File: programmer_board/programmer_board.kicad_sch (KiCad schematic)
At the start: 18 parts, among them J1 8bit_thing_bus_connector, J2 greenpak_i2c, U1 Pico, U2 74AHCT573, U3 74AHCT573, U4 74AHCT573, U5 74LVC245, U6 SLG46826G

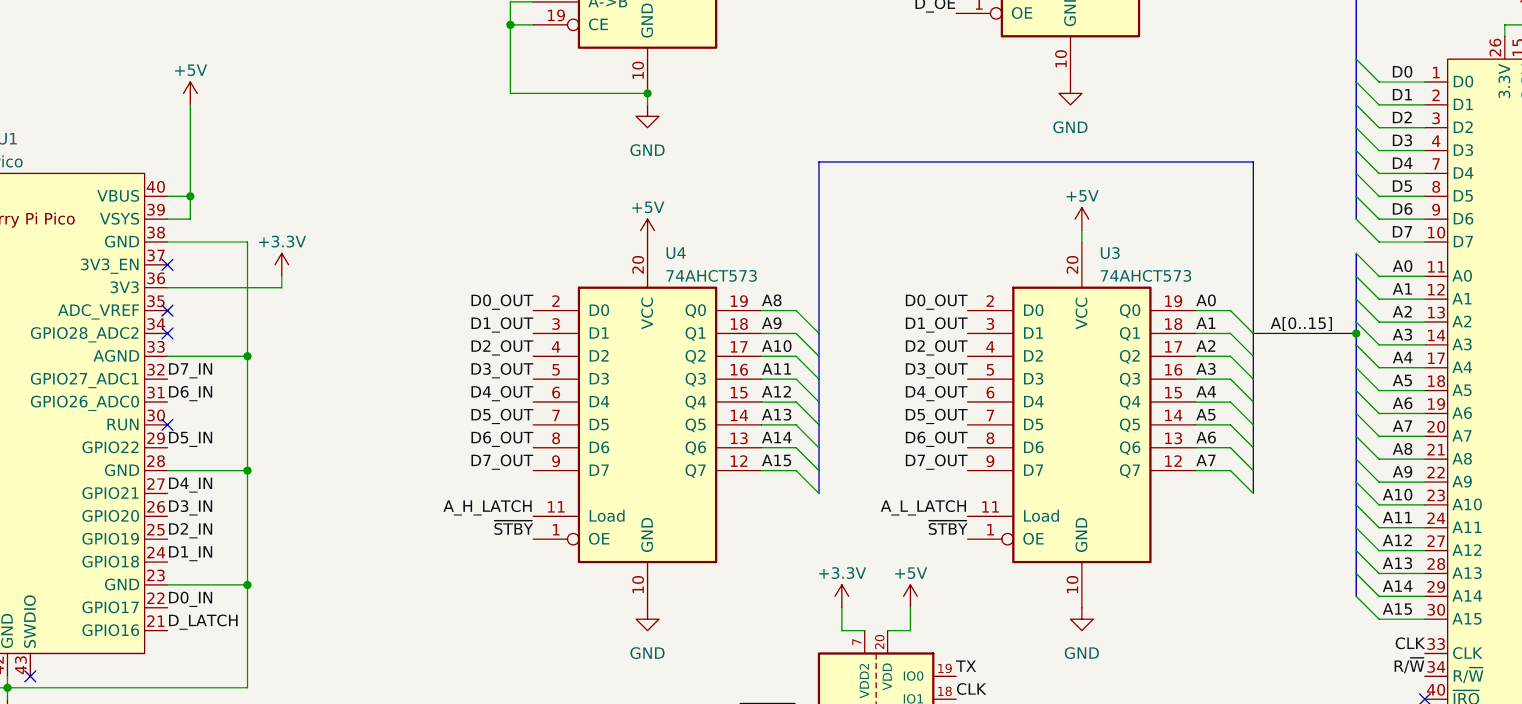
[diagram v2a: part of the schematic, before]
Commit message: pico board: low address latch needs independent OE to not conflict with latch on HD6301 board
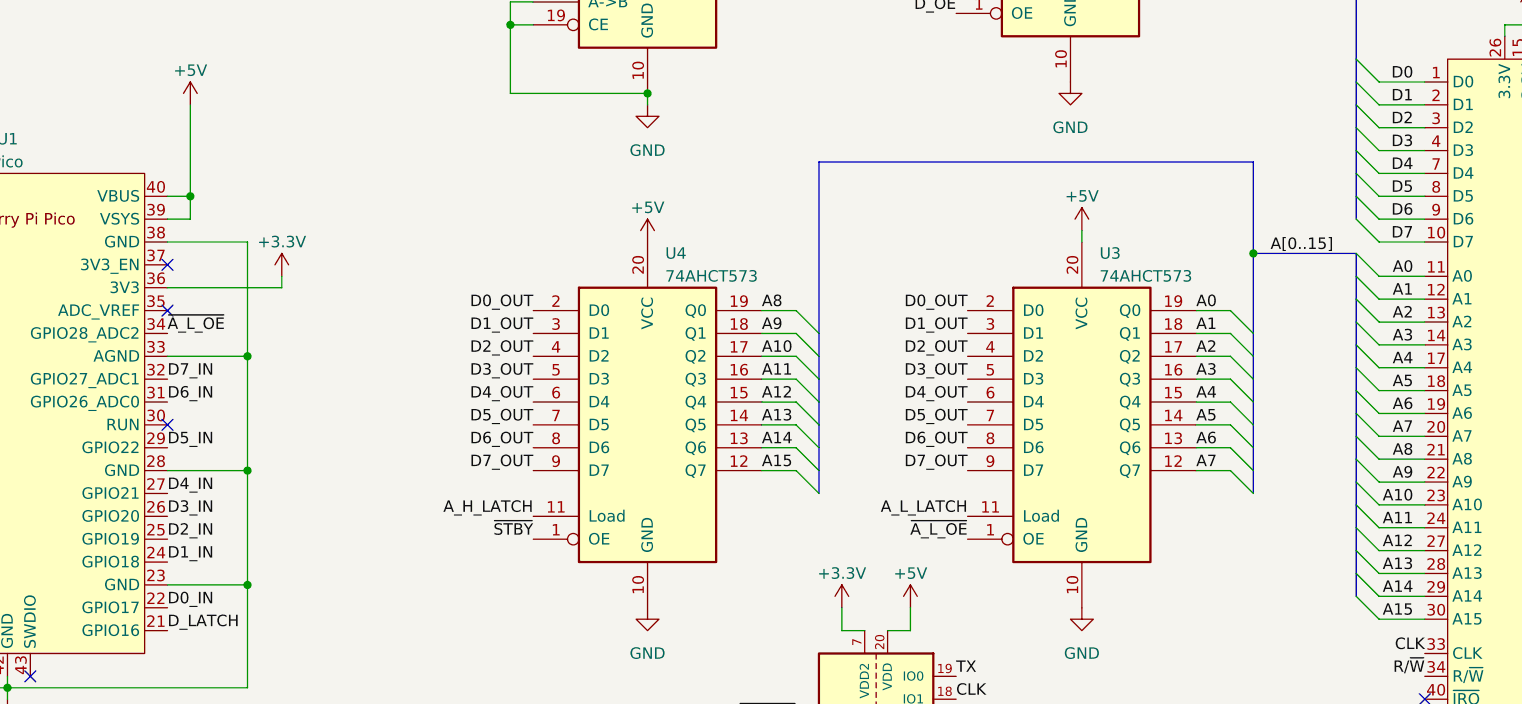
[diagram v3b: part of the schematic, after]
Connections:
- net ~{STBY}: no longer U3.1 (OE)
- net ~{A_L_OE}: now reaches U1.34 (GPIO28_ADC2)
- net ~{A_L_OE}: now also U3.1 (OE)
- no-connect marks 10 -> 9
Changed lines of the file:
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@@
   (junction (at 139.7 57.15) (diameter 0) (color 0 0 0 0)
   )
-  (junction (at 233.68 91.44) (diameter 0) (color 0 0 0 0)
-  )
   (junction (at 252.73 57.15) (diameter 0) (color 0 0 0 0)
   )
@@
   )
   (junction (at 72.39 26.67) (diameter 0) (color 0 0 0 0)
+  )
+  (junction (at 222.25 82.55) (diameter 0) (color 0 0 0 0)
   )
   (junction (at 257.81 57.15) (diameter 0) (color 0 0 0 0)
@@
   (no_connect (at 241.3 134.62))
   (no_connect (at 81.28 129.54))
-  (no_connect (at 101.6 91.44))
   (bus_entry (at 233.68 78.74) (size 2.54 2.54)
     (stroke (width 0) (type default))
@@
     (stroke (width 0) (type default))
   )
-  (bus (pts (xy 222.25 91.44) (xy 233.68 91.44))
+  (bus (pts (xy 222.25 82.55) (xy 233.68 82.55))
     (stroke (width 0) (type default))
   )
@@
     (stroke (width 0) (type default))
   )
-  (bus (pts (xy 233.68 90.17) (xy 233.68 91.44))
-    (stroke (width 0) (type default))
-  )
   (bus (pts (xy 233.68 92.71) (xy 233.68 95.25))
     (stroke (width 0) (type default))
@@
     (stroke (width 0) (type default))
   )
-  (bus (pts (xy 233.68 91.44) (xy 233.68 92.71))
+  (bus (pts (xy 233.68 90.17) (xy 233.68 92.71))
     (stroke (width 0) (type default))
   )
@@
     (stroke (width 0) (type default))
   )
+  (bus (pts (xy 222.25 82.55) (xy 222.25 72.39))
+    (stroke (width 0) (type default))
+  )
   (wire (pts (xy 236.22 87.63) (xy 241.3 87.63))
     (stroke (width 0) (type default))
@@
     (stroke (width 0) (type default))
   )
-  (bus (pts (xy 222.25 91.44) (xy 222.25 72.39))
+  (bus (pts (xy 222.25 91.44) (xy 222.25 82.55))
     (stroke (width 0) (type default))
   )
@@
     (effects (font (size 1.27 1.27)) (justify right bottom))
   )
-  (label "A[0..15]" (at 231.14 91.44 180) (fields_autoplaced)
+  (label "A[0..15]" (at 231.14 82.55 180) (fields_autoplaced)
     (effects (font (size 1.27 1.27)) (justify right bottom))
   )
@@
     (effects (font (size 1.27 1.27)) (justify left bottom))
   )
+  (label "~{A_L_OE}" (at 101.6 91.44 0) (fields_autoplaced)
+    (effects (font (size 1.27 1.27)) (justify left bottom))
+  )
   (label "P_CLK" (at 171.45 137.16 180) (fields_autoplaced)
     (effects (font (size 1.27 1.27)) (justify right bottom))
@@
     (effects (font (size 1.27 1.27)) (justify right bottom))
   )
-  (label "~{STBY}" (at 190.5 114.3 180) (fields_autoplaced)
-    (effects (font (size 1.27 1.27)) (justify right bottom))
-  )
   (label "P_TX" (at 66.04 76.2 180) (fields_autoplaced)
     (effects (font (size 1.27 1.27)) (justify right bottom))
@@
     (effects (font (size 1.27 1.27)) (justify right bottom))
   )
+  (label "~{A_L_OE}" (at 190.5 114.3 180) (fields_autoplaced)
+    (effects (font (size 1.27 1.27)) (justify right bottom))
+  )

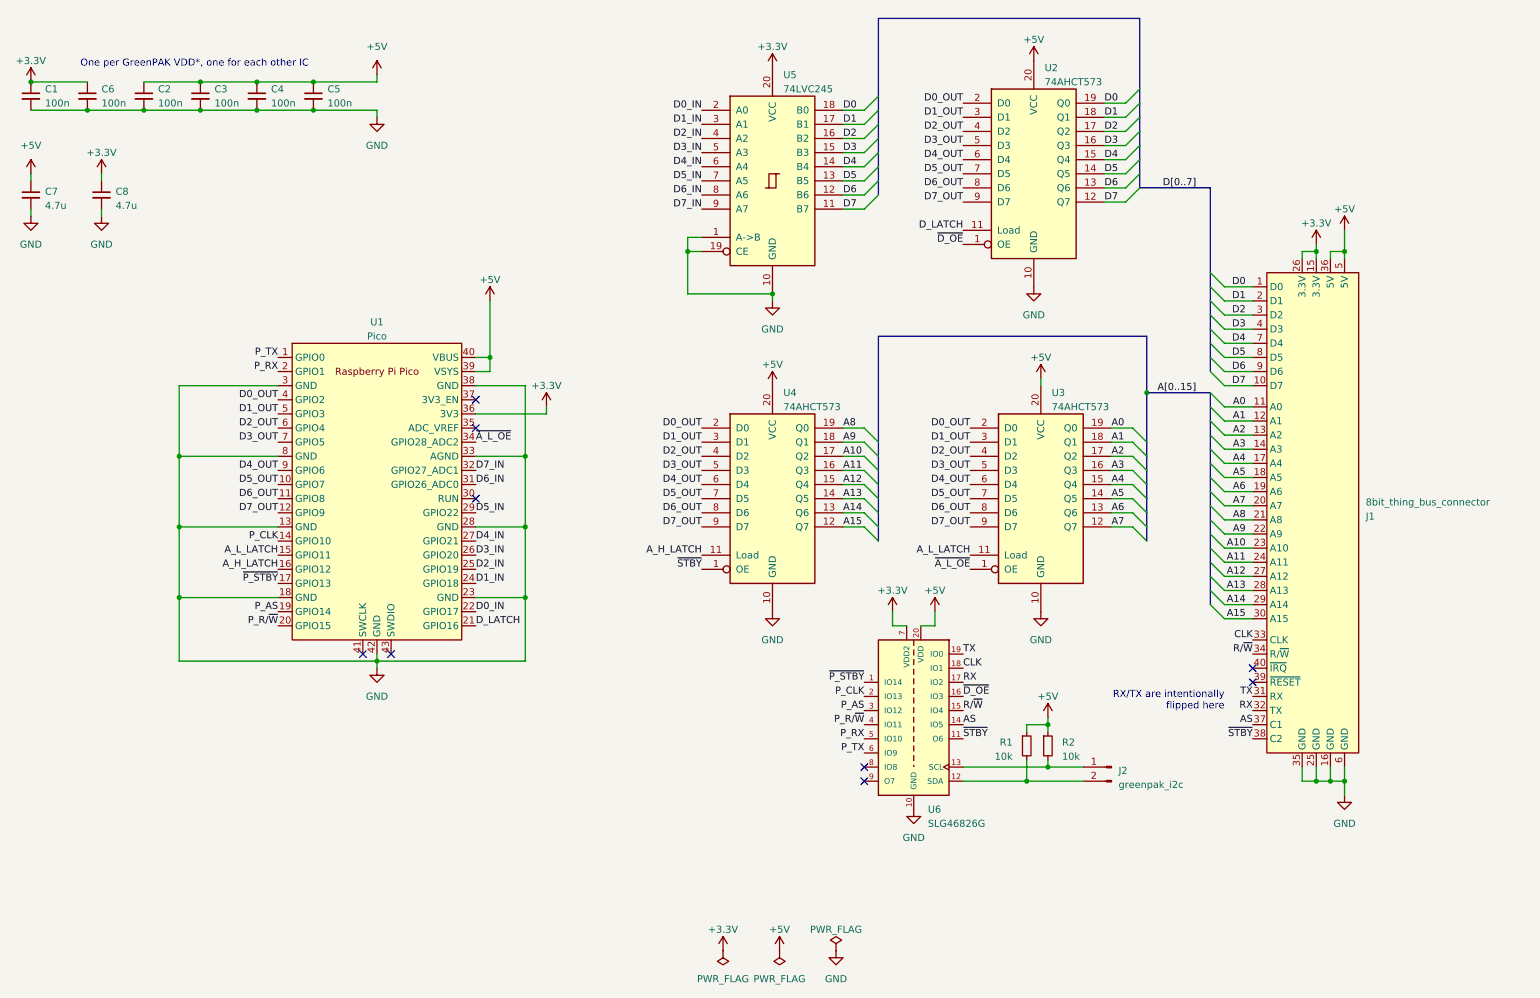
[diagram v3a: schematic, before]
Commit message: Completely reworked Pico programmer v1 board - final version
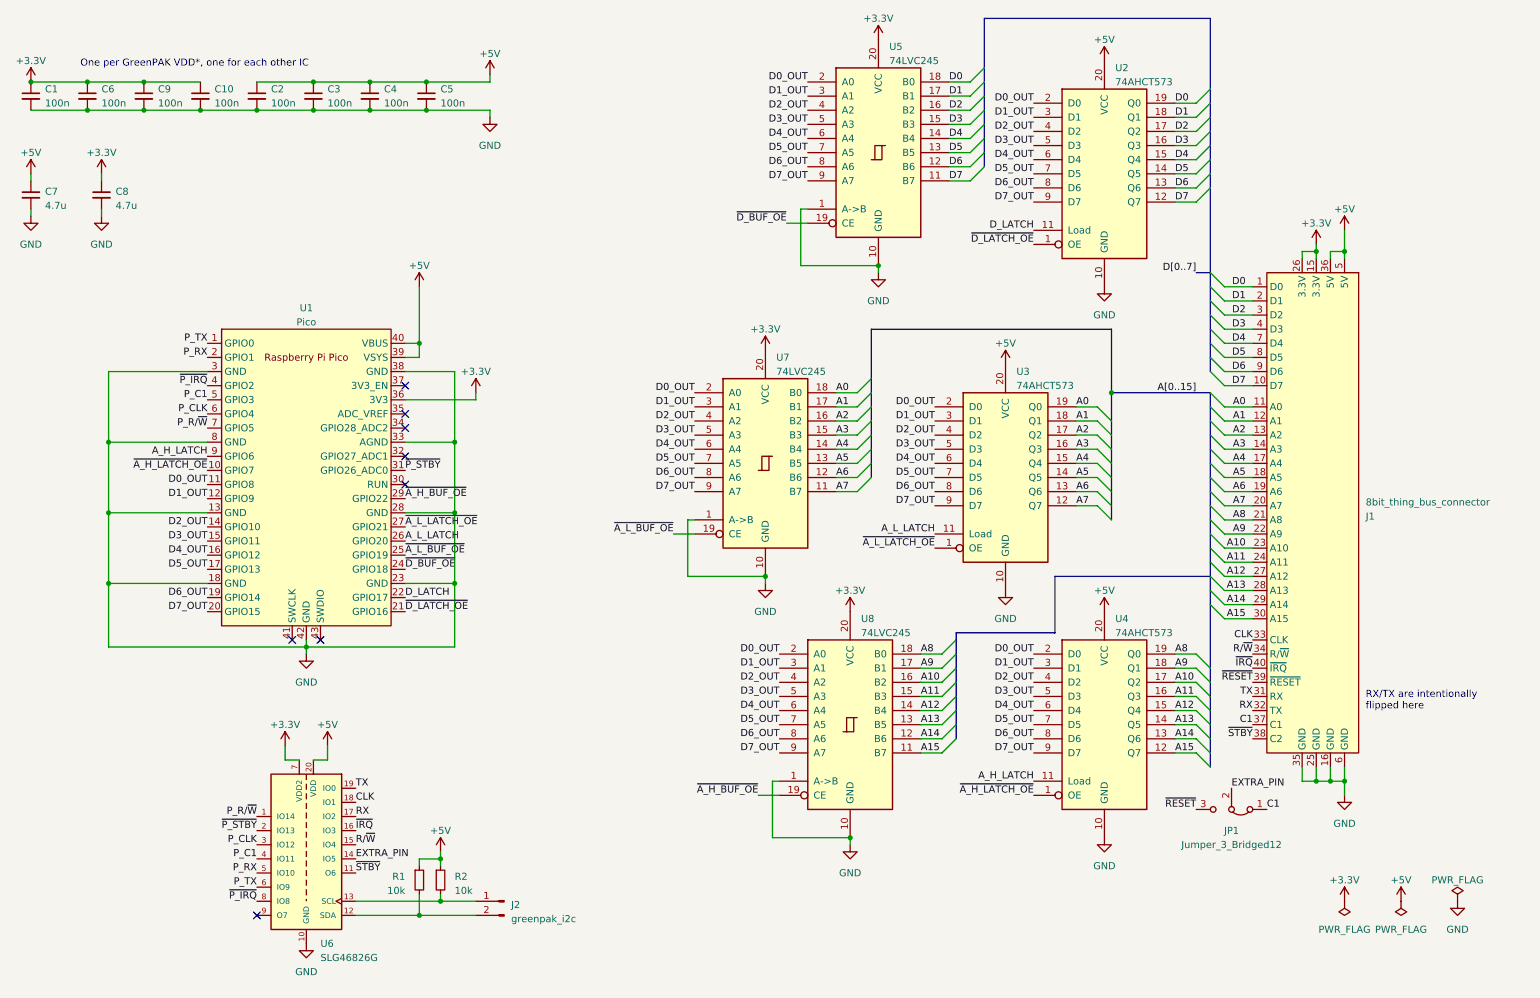
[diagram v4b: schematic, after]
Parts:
- added C10, C9: 100n, Capacitor_SMD:C_0805_2012Metric_Pad1.18x1.45mm_HandSolder, symbol Device:C_Small
- added JP1: Jumper_3_Bridged12, Connector_PinHeader_2.54mm:PinHeader_1x03_P2.54mm_Vertical, symbol Jumper:Jumper_3_Bridged12
- added U7, U8: 74LVC245, Package_SO:TSSOP-20_4.4x6.5mm_P0.65mm, symbol 74xx:74HC245
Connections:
- net +3.3V: now also C10.1, C9.1, U7.20 (VCC), U8.20 (VCC)
- net A0: now also U7.18 (B0)
- net A1: now also U7.17 (B1)
- net A10: now also U8.16 (B2)
- net A11: now also U8.15 (B3)
- net A12: now also U8.14 (B4)
- net A13: now also U8.13 (B5)
- net A14: now also U8.12 (B6)
- net A15: now also U8.11 (B7)
- net A2: now also U7.16 (B2)
- net A3: now also U7.15 (B3)
- net A4: now also U7.14 (B4)
- net A5: now also U7.13 (B5)
- net A6: now also U7.12 (B6)
- net A7: now also U7.11 (B7)
- net A8: now also U8.18 (B0)
- net A9: now also U8.17 (B1)
- net A_H_LATCH: now also U1.9 (GPIO6); no longer U1.16 (GPIO12)
- net A_L_LATCH: now also U1.26 (GPIO20); no longer U1.15 (GPIO11)
- net D0_OUT: now also U1.11 (GPIO8), U5.2 (A0), U7.2 (A0), U8.2 (A0); no longer U1.4 (GPIO2)
- net D1_OUT: now also U1.12 (GPIO9), U5.3 (A1), U7.3 (A1), U8.3 (A1); no longer U1.5 (GPIO3)
- net D2_OUT: now also U1.14 (GPIO10), U5.4 (A2), U7.4 (A2), U8.4 (A2); no longer U1.6 (GPIO4)
- net D3_OUT: now also U1.15 (GPIO11), U5.5 (A3), U7.5 (A3), U8.5 (A3); no longer U1.7 (GPIO5)
- net D4_OUT: now also U1.16 (GPIO12), U5.6 (A4), U7.6 (A4), U8.6 (A4); no longer U1.9 (GPIO6)
- net D5_OUT: now also U1.17 (GPIO13), U5.7 (A5), U7.7 (A5), U8.7 (A5); no longer U1.10 (GPIO7)
- net D6_OUT: now also U1.19 (GPIO14), U5.8 (A6), U7.8 (A6), U8.8 (A6); no longer U1.11 (GPIO8)
- net D7_OUT: now also U1.20 (GPIO15), U5.9 (A7), U7.9 (A7), U8.9 (A7); no longer U1.12 (GPIO9)
- net D_LATCH: now also U1.22 (GPIO17); no longer U1.21 (GPIO16)
- net GND: now also C10.2, C9.2, U7.1 (A->B), U7.10 (GND), U8.1 (A->B), U8.10 (GND); no longer U5.19 (CE)
- net P_CLK: now also U1.6 (GPIO4), U6.3 (IO12); no longer U1.14 (GPIO10), U6.2 (IO13)
- net P_R/~{W}: now also U1.7 (GPIO5), U6.1 (IO14); no longer U1.20 (GPIO15), U6.4 (IO11)
- net ~{P_STBY}: now also U1.31 (GPIO26_ADC0), U6.2 (IO13); no longer U1.17 (GPIO13), U6.1 (IO14)
- net ~{STBY}: no longer U4.1 (OE)
- net ~{P_IRQ}: now reaches U6.8 (IO8)
- net ~{P_IRQ}: now also U1.4 (GPIO2)
- net ~{RESET}: now reaches J1.39 (~{RESET})
- net ~{RESET}: now also JP1.3 (B)
- net ~{IRQ}: now reaches J1.40 (~{IRQ})
- net ~{IRQ}: now also U6.16 (IO3)
- net AS renamed C1
- net C1: now also JP1.1 (A); no longer U6.14 (IO5)
- removed net D0_IN: U1.22 (GPIO17), U5.2 (A0)
- net D1_IN renamed ~{D_BUF_OE}
- net ~{D_BUF_OE}: now also U5.19 (CE); no longer U5.3 (A1)
- net D2_IN renamed ~{A_L_BUF_OE}
- net ~{A_L_BUF_OE}: now also U7.19 (CE); no longer U5.4 (A2)
- removed net D3_IN: U1.26 (GPIO20), U5.5 (A3)
- net D4_IN renamed ~{A_L_LATCH_OE}
- net ~{A_L_LATCH_OE}: now also U3.1 (OE); no longer U5.6 (A4)
- net D5_IN renamed ~{A_H_BUF_OE}
- net ~{A_H_BUF_OE}: now also U8.19 (CE); no longer U5.7 (A5)
- removed net D6_IN: U1.31 (GPIO26_ADC0), U5.8 (A6)
- net D7_IN: no longer names the net of U1.32 (GPIO27_ADC1)
- net D7_IN: no longer U5.9 (A7)
- removed net P_AS: U1.19 (GPIO14), U6.3 (IO12)
- net ~{A_L_OE}: no longer names the net of U1.34 (GPIO28_ADC2)
- net ~{A_L_OE}: no longer U3.1 (OE)
- net ~{D_OE} renamed ~{D_LATCH_OE}
- net ~{D_LATCH_OE}: now also U1.21 (GPIO16); no longer U6.16 (IO3)
- new net EXTRA_PIN: JP1.2 (C), U6.14 (IO5)
- new net P_C1: U1.5 (GPIO3), U6.4 (IO11)
- new net ~{A_H_LATCH_OE}: U1.10 (GPIO7), U4.1 (OE)
- no-connect marks 9 -> 8
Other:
- moved on the sheet: C2, C3, C4, C5, J2, R1, R2, U1, U2, U3, U4, U5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
